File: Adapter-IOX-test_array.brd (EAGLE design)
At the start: 111.8 x 111.8 mm, 204 parts, among them Q0X11 P-FET, Q0X12 P-FET, Q0X13 P-FET, Q0X14 P-FET, Q10X11 P-FET, Q10X12 P-FET, Q10X13 P-FET, Q10X14 P-FET, Q11X11 P-FET, Q11X12 P-FET, Q11X13 P-FET, Q11X14 P-FET, Q12X11 P-FET, Q12X12 P-FET, Q12X13 P-FET, Q12X14 P-FET, Q13X11 P-FET, Q13X12 P-FET, Q13X13 P-FET, Q13X14 P-FET, Q14X11 P-FET, Q14X12 P-FET, Q14X13 P-FET, Q14X14 P-FET, Q15X11 P-FET, Q15X12 P-FET, Q15X13 P-FET, Q15X14 P-FET, Q1X11 P-FET, Q1X12 P-FET, Q1X13 P-FET, Q1X14 P-FET, Q2X11 P-FET, Q2X12 P-FET, Q2X13 P-FET, Q2X14 P-FET, Q3X11 P-FET, Q3X12 P-FET, Q3X13 P-FET, Q3X14 P-FET, Q4X11 P-FET, Q4X12 P-FET, Q4X13 P-FET, Q4X14 P-FET, Q5X11 P-FET, Q5X12 P-FET, Q5X13 P-FET, Q5X14 P-FET, Q6X11 P-FET, Q6X12 P-FET, Q6X13 P-FET, Q6X14 P-FET, Q7X11 P-FET, Q7X12 P-FET, Q7X13 P-FET, Q7X14 P-FET, Q8X11 P-FET, Q8X12 P-FET, Q8X13 P-FET, Q8X14 P-FET, Q9X11 P-FET, Q9X12 P-FET, Q9X13 P-FET, Q9X14 P-FET

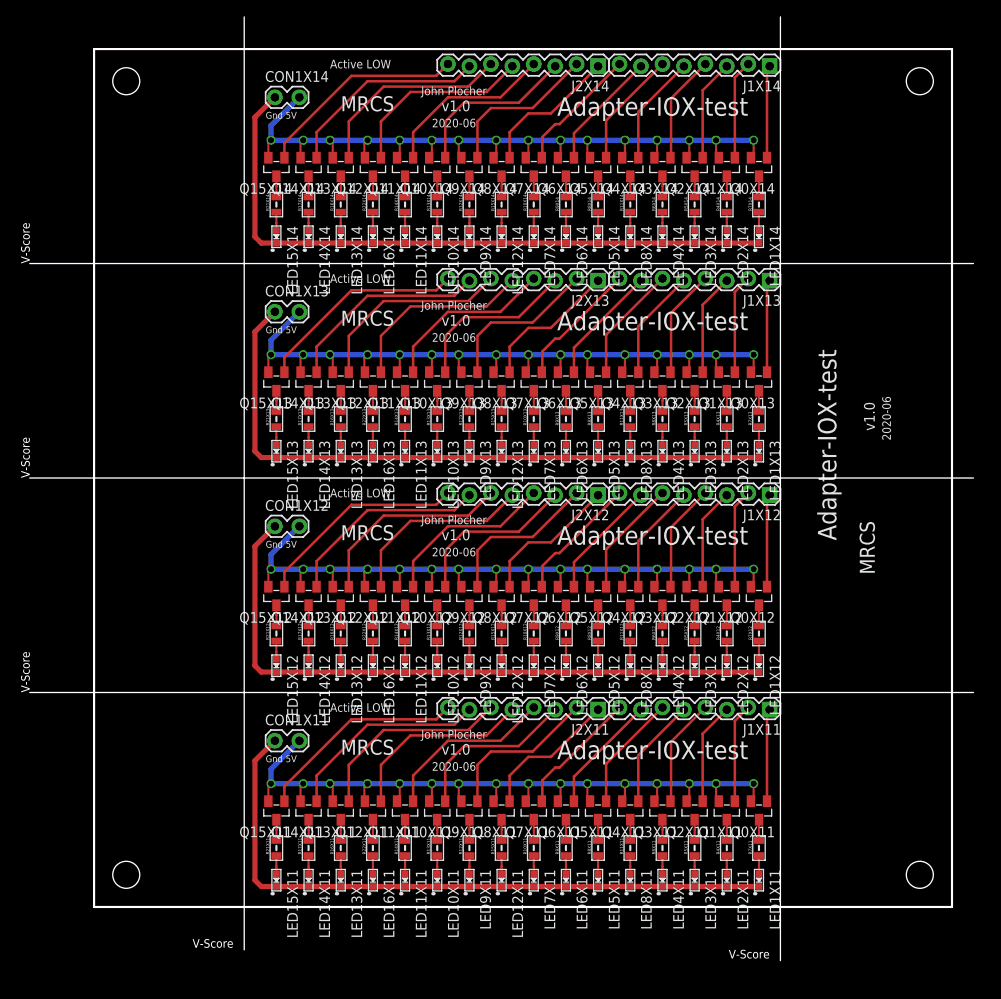
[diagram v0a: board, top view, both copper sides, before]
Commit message: higher density, narrow the board so 2x work with IOX-32
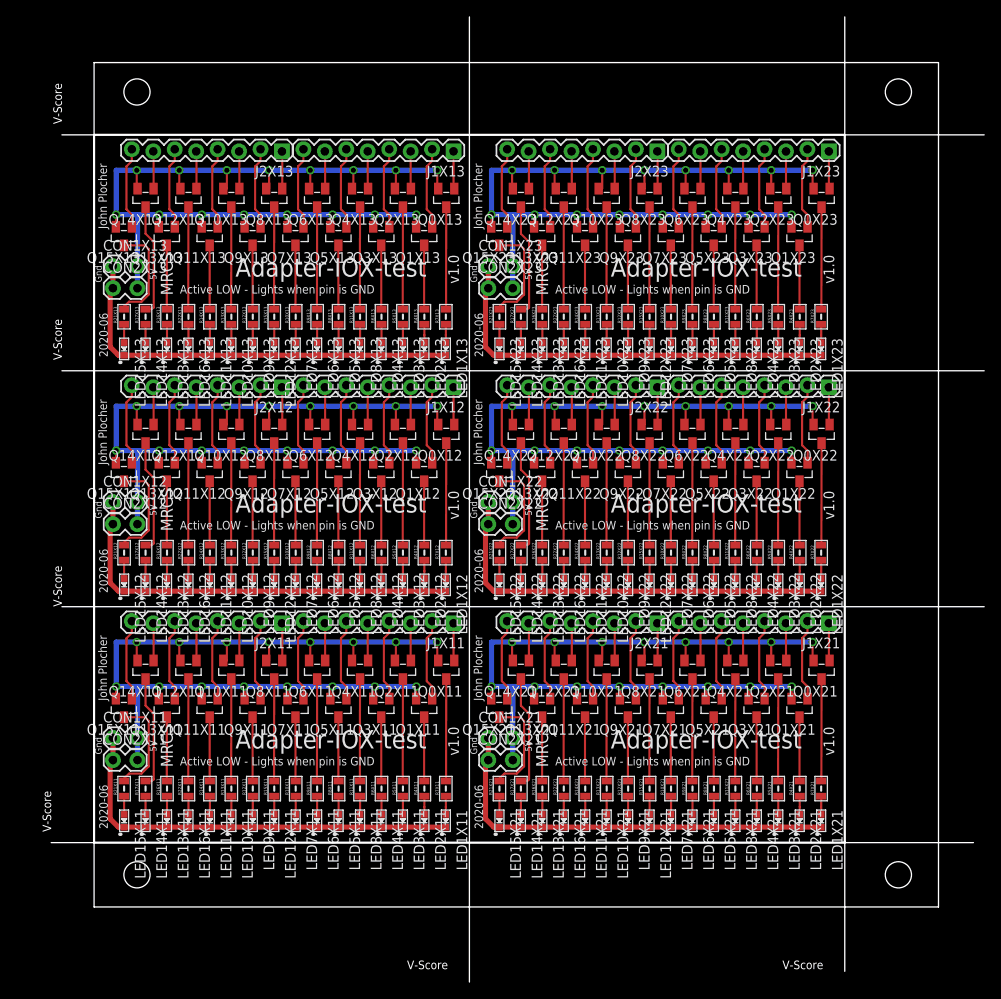
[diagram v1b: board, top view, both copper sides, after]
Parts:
- removed CON1X14: (no value), SPCoast:1X02_LOCK
- removed J1X14, J2X14: (no value), SPCoast:1X08_LOCK
- removed LED10X14, LED11X14, LED12X14, LED13X14, LED14X14, LED15X14, LED16X14, LED1X14, LED2X14, LED3X14, LED4X14, LED5X14, LED6X14, LED7X14, LED8X14, LED9X14: Y, SPCoast:0603-LED
- removed Q0X14, Q10X14, Q11X14, Q12X14, Q13X14, Q14X14, Q15X14, Q1X14, Q2X14, Q3X14, Q4X14, Q5X14, Q6X14, Q7X14, Q8X14, Q9X14: P-FET, SPCoast:SOT23
- removed R10X14, R11X14, R12X14, R13X14, R14X14, R15X14, R16X14, R17X14, R21X14, R22X14, R4X14, R5X14, R6X14, R7X14, R8X14, R9X14: 2K0, SPCoast:0805-RES
- added CON1X21, CON1X22, CON1X23, CON2X11, CON2X12, CON2X13, CON2X21, CON2X22, CON2X23: (no value), SPCoast:1X02_LOCK
- added J1X21, J1X22, J1X23, J2X21, J2X22, J2X23: (no value), SPCoast:1X08_LOCK
- added LED10X21, LED10X22, LED10X23, LED11X21, LED11X22, LED11X23, LED12X21, LED12X22, LED12X23, LED13X21, LED13X22, LED13X23, LED14X21, LED14X22, LED14X23, LED15X21, LED15X22, LED15X23, LED16X21, LED16X22, LED16X23, LED1X21, LED1X22, LED1X23, LED2X21, LED2X22, LED2X23, LED3X21, LED3X22, LED3X23, LED4X21, LED4X22, LED4X23, LED5X21, LED5X22, LED5X23, LED6X21, LED6X22, LED6X23, LED7X21, LED7X22, LED7X23, LED8X21, LED8X22, LED8X23, LED9X21, LED9X22, LED9X23: Y, SPCoast:0603-LED
- added Q0X21, Q0X22, Q0X23, Q10X21, Q10X22, Q10X23, Q11X21, Q11X22, Q11X23, Q12X21, Q12X22, Q12X23, Q13X21, Q13X22, Q13X23, Q14X21, Q14X22, Q14X23, Q15X21, Q15X22, Q15X23, Q1X21, Q1X22, Q1X23, Q2X21, Q2X22, Q2X23, Q3X21, Q3X22, Q3X23, Q4X21, Q4X22, Q4X23, Q5X21, Q5X22, Q5X23, Q6X21, Q6X22, Q6X23, Q7X21, Q7X22, Q7X23, Q8X21, Q8X22, Q8X23, Q9X21, Q9X22, Q9X23: P-FET, SPCoast:SOT23
- added R10X21, R10X22, R10X23, R11X21, R11X22, R11X23, R12X21, R12X22, R12X23, R13X21, R13X22, R13X23, R14X21, R14X22, R14X23, R15X21, R15X22, R15X23, R16X21, R16X22, R16X23, R17X21, R17X22, R17X23, R21X21, R21X22, R21X23, R22X21, R22X22, R22X23, R4X21, R4X22, R4X23, R5X21, R5X22, R5X23, R6X21, R6X22, R6X23, R7X21, R7X22, R7X23, R8X21, R8X22, R8X23, R9X21, R9X22, R9X23: 2K0, SPCoast:0805-RES
- added R22X1: (no value), SPCoast:BOARD-10X10-TEMPLATE
- moved Q0X13 42.9 mm to (41.7, 84.0)
- moved Q0X12 41.7 mm to (41.7, 56.0)
- moved Q2X13 40.8 mm to (36.6, 84.0)
- moved Q0X11 40.6 mm to (41.7, 28.1)
- moved J1X13 40.5 mm to (42.6, 89.6)
- moved J2X13 40.5 mm to (22.3, 89.6)
- moved Q1X13 39.8 mm to (39.1, 79.5)
- moved J1X12 39.6 mm to (42.6, 61.7)
- moved J2X12 39.6 mm to (22.3, 61.7)
- moved Q2X12 39.5 mm to (36.6, 56.0)
- moved LED1X13 39.0 mm to (41.7, 66.1)
- moved R7X13 39.0 mm to (41.7, 69.9)
- moved J1X11 38.8 mm to (42.6, 33.7)
- moved J2X11 38.8 mm to (22.3, 33.7)
- moved Q1X12 38.7 mm to (39.1, 51.5)
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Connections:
- removed net GNDX14: CON1X14.1, LED10X14.C, LED11X14.C, LED12X14.C, LED13X14.C, LED14X14.C, LED15X14.C, LED16X14.C, LED1X14.C, LED2X14.C, LED3X14.C, LED4X14.C, LED5X14.C, LED6X14.C, LED7X14.C, LED8X14.C, LED9X14.C
- removed net N$10X14: Q8X14.3, R15X14.2
- removed net N$11X14: Q9X14.3, R12X14.2
- removed net N$12X14: Q10X14.3, R13X14.2
- removed net N$13X14: Q11X14.3, R14X14.2
- removed net N$14X14: LED12X14.A, R15X14.1
- removed net N$15X14: LED9X14.A, R12X14.1
- removed net N$1X14: Q4X14.3, R11X14.2
- removed net N$23X14: LED10X14.A, R13X14.1
- removed net N$24X14: LED11X14.A, R14X14.1
- removed net N$28X14: Q12X14.3, R22X14.2
- removed net N$29X14: Q13X14.3, R16X14.2
- removed net N$30X14: Q14X14.3, R17X14.2
- removed net N$31X14: Q15X14.3, R21X14.2
- removed net N$32X14: LED16X14.A, R22X14.1
- removed net N$33X14: LED13X14.A, R16X14.1
- removed net N$34X14: LED14X14.A, R17X14.1
- removed net N$35X14: LED15X14.A, R21X14.1
- removed net N$3X14: Q5X14.3, R8X14.2
- removed net N$44X14: Q0X14.3, R7X14.2
- removed net N$45X14: Q1X14.3, R4X14.2
- removed net N$46X14: Q2X14.3, R5X14.2
- removed net N$47X14: Q3X14.3, R6X14.2
- removed net N$48X14: LED1X14.A, R7X14.1
- removed net N$49X14: LED2X14.A, R4X14.1
- removed net N$4X14: Q6X14.3, R9X14.2
- removed net N$50X14: LED3X14.A, R5X14.1
- removed net N$51X14: LED4X14.A, R6X14.1
- removed net N$5X14: Q7X14.3, R10X14.2
- removed net N$6X14: LED8X14.A, R11X14.1
- removed net N$7X14: LED5X14.A, R8X14.1
- removed net N$8X14: LED6X14.A, R9X14.1
- removed net N$9X14: LED7X14.A, R10X14.1
- removed net P10X14: J2X14.2, Q9X14.1
- removed net P11X14: J2X14.3, Q10X14.1
- removed net P12X14: J2X14.4, Q11X14.1
- removed net P13X14: J2X14.5, Q12X14.1
- removed net P14X14: J2X14.6, Q13X14.1
- removed net P15X14: J2X14.7, Q14X14.1
- removed net P16X14: J2X14.8, Q15X14.1
- removed net P1X14: J1X14.1, Q0X14.1
- removed net P2X14: J1X14.2, Q1X14.1
- removed net P3X14: J1X14.3, Q2X14.1
- removed net P4X14: J1X14.4, Q3X14.1
- removed net P5X14: J1X14.5, Q4X14.1
- removed net P6X14: J1X14.6, Q5X14.1
- removed net P7X14: J1X14.7, Q6X14.1
- removed net P8X14: J1X14.8, Q7X14.1
- removed net P9X14: J2X14.1, Q8X14.1
- removed net VCCX14: CON1X14.2, Q0X14.2, Q10X14.2, Q11X14.2, Q12X14.2, Q13X14.2, Q14X14.2, Q15X14.2, Q1X14.2, Q2X14.2, Q3X14.2, Q4X14.2, Q5X14.2, Q6X14.2, Q7X14.2, Q8X14.2, Q9X14.2
- new net GNDX21: CON1X21.1, CON2X21.1, LED10X21.C, LED11X21.C, LED12X21.C, LED13X21.C, LED14X21.C, LED15X21.C, LED16X21.C, LED1X21.C, LED2X21.C, LED3X21.C, LED4X21.C, LED5X21.C, LED6X21.C, LED7X21.C, LED8X21.C, LED9X21.C
- new net GNDX22: CON1X22.1, CON2X22.1, LED10X22.C, LED11X22.C, LED12X22.C, LED13X22.C, LED14X22.C, LED15X22.C, LED16X22.C, LED1X22.C, LED2X22.C, LED3X22.C, LED4X22.C, LED5X22.C, LED6X22.C, LED7X22.C, LED8X22.C, LED9X22.C
- new net GNDX23: CON1X23.1, CON2X23.1, LED10X23.C, LED11X23.C, LED12X23.C, LED13X23.C, LED14X23.C, LED15X23.C, LED16X23.C, LED1X23.C, LED2X23.C, LED3X23.C, LED4X23.C, LED5X23.C, LED6X23.C, LED7X23.C, LED8X23.C, LED9X23.C
- new net N$10X21: Q8X21.3, R15X21.2
- new net N$10X22: Q8X22.3, R15X22.2
- new net N$10X23: Q8X23.3, R15X23.2
- new net N$11X21: Q9X21.3, R12X21.2
- new net N$11X22: Q9X22.3, R12X22.2
- new net N$11X23: Q9X23.3, R12X23.2
- new net N$12X21: Q10X21.3, R13X21.2
- new net N$12X22: Q10X22.3, R13X22.2
- new net N$12X23: Q10X23.3, R13X23.2
- new net N$13X21: Q11X21.3, R14X21.2
- new net N$13X22: Q11X22.3, R14X22.2
- new net N$13X23: Q11X23.3, R14X23.2
- new net N$14X21: LED12X21.A, R15X21.1
- new net N$14X22: LED12X22.A, R15X22.1
- new net N$14X23: LED12X23.A, R15X23.1
- new net N$15X21: LED9X21.A, R12X21.1
- new net N$15X22: LED9X22.A, R12X22.1
- new net N$15X23: LED9X23.A, R12X23.1
- new net N$1X21: Q4X21.3, R11X21.2
- new net N$1X22: Q4X22.3, R11X22.2
- new net N$1X23: Q4X23.3, R11X23.2
- new net N$23X21: LED10X21.A, R13X21.1
- new net N$23X22: LED10X22.A, R13X22.1
- new net N$23X23: LED10X23.A, R13X23.1
- new net N$24X21: LED11X21.A, R14X21.1
- new net N$24X22: LED11X22.A, R14X22.1
- new net N$24X23: LED11X23.A, R14X23.1
- new net N$28X21: Q12X21.3, R22X21.2
- new net N$28X22: Q12X22.3, R22X22.2
- new net N$28X23: Q12X23.3, R22X23.2
- new net N$29X21: Q13X21.3, R16X21.2
- new net N$29X22: Q13X22.3, R16X22.2
- new net N$29X23: Q13X23.3, R16X23.2
- new net N$30X21: Q14X21.3, R17X21.2
- new net N$30X22: Q14X22.3, R17X22.2
- new net N$30X23: Q14X23.3, R17X23.2
- new net N$31X21: Q15X21.3, R21X21.2
- new net N$31X22: Q15X22.3, R21X22.2
- new net N$31X23: Q15X23.3, R21X23.2
- new net N$32X21: LED16X21.A, R22X21.1
- new net N$32X22: LED16X22.A, R22X22.1
- new net N$32X23: LED16X23.A, R22X23.1
- new net N$33X21: LED13X21.A, R16X21.1
- new net N$33X22: LED13X22.A, R16X22.1
- new net N$33X23: LED13X23.A, R16X23.1
- new net N$34X21: LED14X21.A, R17X21.1
- new net N$34X22: LED14X22.A, R17X22.1
- new net N$34X23: LED14X23.A, R17X23.1
- new net N$35X21: LED15X21.A, R21X21.1
- new net N$35X22: LED15X22.A, R21X22.1
- new net N$35X23: LED15X23.A, R21X23.1
- new net N$3X21: Q5X21.3, R8X21.2
- new net N$3X22: Q5X22.3, R8X22.2
- new net N$3X23: Q5X23.3, R8X23.2
- new net N$44X21: Q0X21.3, R7X21.2
- new net N$44X22: Q0X22.3, R7X22.2
- new net N$44X23: Q0X23.3, R7X23.2
- new net N$45X21: Q1X21.3, R4X21.2
- new net N$45X22: Q1X22.3, R4X22.2
- new net N$45X23: Q1X23.3, R4X23.2
- new net N$46X21: Q2X21.3, R5X21.2
- new net N$46X22: Q2X22.3, R5X22.2
- new net N$46X23: Q2X23.3, R5X23.2
- new net N$47X21: Q3X21.3, R6X21.2
- new net N$47X22: Q3X22.3, R6X22.2
- new net N$47X23: Q3X23.3, R6X23.2
- new net N$48X21: LED1X21.A, R7X21.1
- new net N$48X22: LED1X22.A, R7X22.1
- new net N$48X23: LED1X23.A, R7X23.1
- new net N$49X21: LED2X21.A, R4X21.1
- new net N$49X22: LED2X22.A, R4X22.1
- new net N$49X23: LED2X23.A, R4X23.1
- new net N$4X21: Q6X21.3, R9X21.2
- new net N$4X22: Q6X22.3, R9X22.2
- new net N$4X23: Q6X23.3, R9X23.2
- new net N$50X21: LED3X21.A, R5X21.1
- new net N$50X22: LED3X22.A, R5X22.1
- new net N$50X23: LED3X23.A, R5X23.1
- new net N$51X21: LED4X21.A, R6X21.1
- new net N$51X22: LED4X22.A, R6X22.1
- new net N$51X23: LED4X23.A, R6X23.1
- new net N$5X21: Q7X21.3, R10X21.2
- new net N$5X22: Q7X22.3, R10X22.2
- new net N$5X23: Q7X23.3, R10X23.2
- new net N$6X21: LED8X21.A, R11X21.1
- new net N$6X22: LED8X22.A, R11X22.1
- new net N$6X23: LED8X23.A, R11X23.1
- new net N$7X21: LED5X21.A, R8X21.1
- new net N$7X22: LED5X22.A, R8X22.1
- new net N$7X23: LED5X23.A, R8X23.1
- new net N$8X21: LED6X21.A, R9X21.1
- new net N$8X22: LED6X22.A, R9X22.1
- new net N$8X23: LED6X23.A, R9X23.1
- new net N$9X21: LED7X21.A, R10X21.1
- new net N$9X22: LED7X22.A, R10X22.1
- new net N$9X23: LED7X23.A, R10X23.1
- new net P10X21: J2X21.2, Q9X21.1
- new net P10X22: J2X22.2, Q9X22.1
- new net P10X23: J2X23.2, Q9X23.1
- new net P11X21: J2X21.3, Q10X21.1
- new net P11X22: J2X22.3, Q10X22.1
- new net P11X23: J2X23.3, Q10X23.1
- new net P12X21: J2X21.4, Q11X21.1
- new net P12X22: J2X22.4, Q11X22.1
- new net P12X23: J2X23.4, Q11X23.1
- new net P13X21: J2X21.5, Q12X21.1
- new net P13X22: J2X22.5, Q12X22.1
- new net P13X23: J2X23.5, Q12X23.1
- new net P14X21: J2X21.6, Q13X21.1
- new net P14X22: J2X22.6, Q13X22.1
- new net P14X23: J2X23.6, Q13X23.1
- new net P15X21: J2X21.7, Q14X21.1
- new net P15X22: J2X22.7, Q14X22.1
- new net P15X23: J2X23.7, Q14X23.1
- new net P16X21: J2X21.8, Q15X21.1
- new net P16X22: J2X22.8, Q15X22.1
- new net P16X23: J2X23.8, Q15X23.1
- new net P1X21: J1X21.1, Q0X21.1
- new net P1X22: J1X22.1, Q0X22.1
- new net P1X23: J1X23.1, Q0X23.1
- new net P2X21: J1X21.2, Q1X21.1
- new net P2X22: J1X22.2, Q1X22.1
- new net P2X23: J1X23.2, Q1X23.1
- new net P3X21: J1X21.3, Q2X21.1
- new net P3X22: J1X22.3, Q2X22.1
- new net P3X23: J1X23.3, Q2X23.1
- new net P4X21: J1X21.4, Q3X21.1
- new net P4X22: J1X22.4, Q3X22.1
- new net P4X23: J1X23.4, Q3X23.1
- new net P5X21: J1X21.5, Q4X21.1
- new net P5X22: J1X22.5, Q4X22.1
- new net P5X23: J1X23.5, Q4X23.1
- new net P6X21: J1X21.6, Q5X21.1
- new net P6X22: J1X22.6, Q5X22.1
- new net P6X23: J1X23.6, Q5X23.1
- new net P7X21: J1X21.7, Q6X21.1
- new net P7X22: J1X22.7, Q6X22.1
- new net P7X23: J1X23.7, Q6X23.1
- new net P8X21: J1X21.8, Q7X21.1
- new net P8X22: J1X22.8, Q7X22.1
- new net P8X23: J1X23.8, Q7X23.1
- new net P9X21: J2X21.1, Q8X21.1
- new net P9X22: J2X22.1, Q8X22.1
- new net P9X23: J2X23.1, Q8X23.1
- new net VCCX21: CON1X21.2, CON2X21.2, Q0X21.2, Q10X21.2, Q11X21.2, Q12X21.2, Q13X21.2, Q14X21.2, Q15X21.2, Q1X21.2, Q2X21.2, Q3X21.2, Q4X21.2, Q5X21.2, Q6X21.2, Q7X21.2, Q8X21.2, Q9X21.2
- new net VCCX22: CON1X22.2, CON2X22.2, Q0X22.2, Q10X22.2, Q11X22.2, Q12X22.2, Q13X22.2, Q14X22.2, Q15X22.2, Q1X22.2, Q2X22.2, Q3X22.2, Q4X22.2, Q5X22.2, Q6X22.2, Q7X22.2, Q8X22.2, Q9X22.2
- new net VCCX23: CON1X23.2, CON2X23.2, Q0X23.2, Q10X23.2, Q11X23.2, Q12X23.2, Q13X23.2, Q14X23.2, Q15X23.2, Q1X23.2, Q2X23.2, Q3X23.2, Q4X23.2, Q5X23.2, Q6X23.2, Q7X23.2, Q8X23.2, Q9X23.2
- net GNDX11: now also CON2X11.1
- net GNDX12: now also CON2X12.1
- net GNDX13: now also CON2X13.1
- net VCCX11: now also CON2X11.2
- net VCCX12: now also CON2X12.2
- net VCCX13: now also CON2X13.2
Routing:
- net VCCX22: track 0.00 -> 118.6 mm, vias 0 -> 16
- net VCCX23: track 0.00 -> 118.6 mm, vias 0 -> 16
- net VCCX21: track 0.00 -> 118.6 mm, vias 0 -> 16
- net VCCX14: track 112.6 -> 0.00 mm, vias 16 -> 0
- net GNDX14: track 77.5 -> 0.00 mm
- net GNDX23: track 0.00 -> 50.0 mm
- net GNDX22: track 0.00 -> 50.0 mm
- net GNDX21: track 0.00 -> 50.0 mm
- net GNDX11: track 77.5 -> 50.0 mm
- net GNDX13: track 77.5 -> 50.0 mm
- net GNDX12: track 77.5 -> 50.0 mm
- net P16X14: track 25.1 -> 0.00 mm
- net P15X14: track 24.4 -> 0.00 mm
- net P14X14: track 23.9 -> 0.00 mm
- net P13X14: track 22.6 -> 0.00 mm
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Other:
- board size 111.8 x 111.8 mm -> 110.5 x 114.3 mm
- board text added: "5V"
- board text added: "5V GND"
- board text added: "Active LOW - Lights when pin is GND"
- board text added: "Gnd"
- board text removed: "Active LOW"
- board text removed: "Gnd 5V"

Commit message: updated docs
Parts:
- added FID1, FID2, FID3, FID4: (no value), SPCoast:FIDUCIAL_1MM
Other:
- outline, holes or cut-outs redrawn
- board text added: "(0,0)"
- board text added: "Feed"

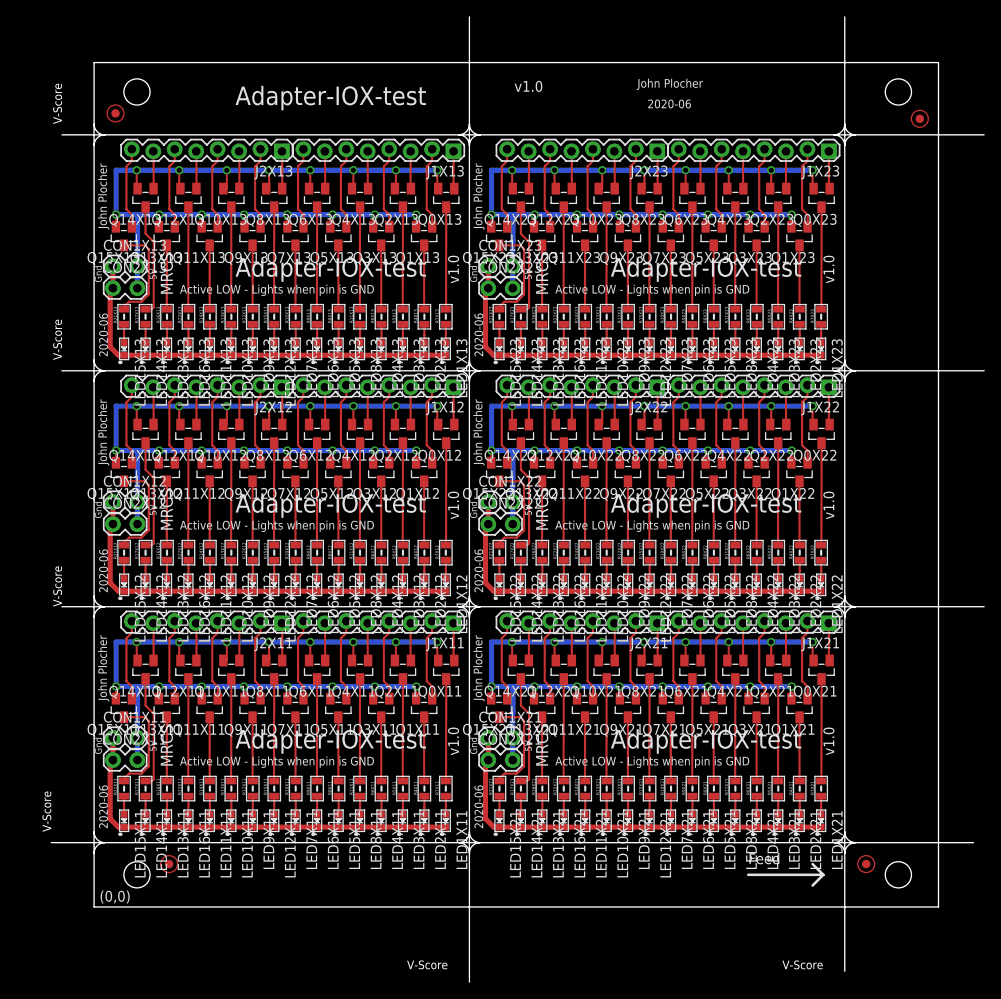
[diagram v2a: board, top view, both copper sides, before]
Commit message: fixed SPCoast lbr part orientation
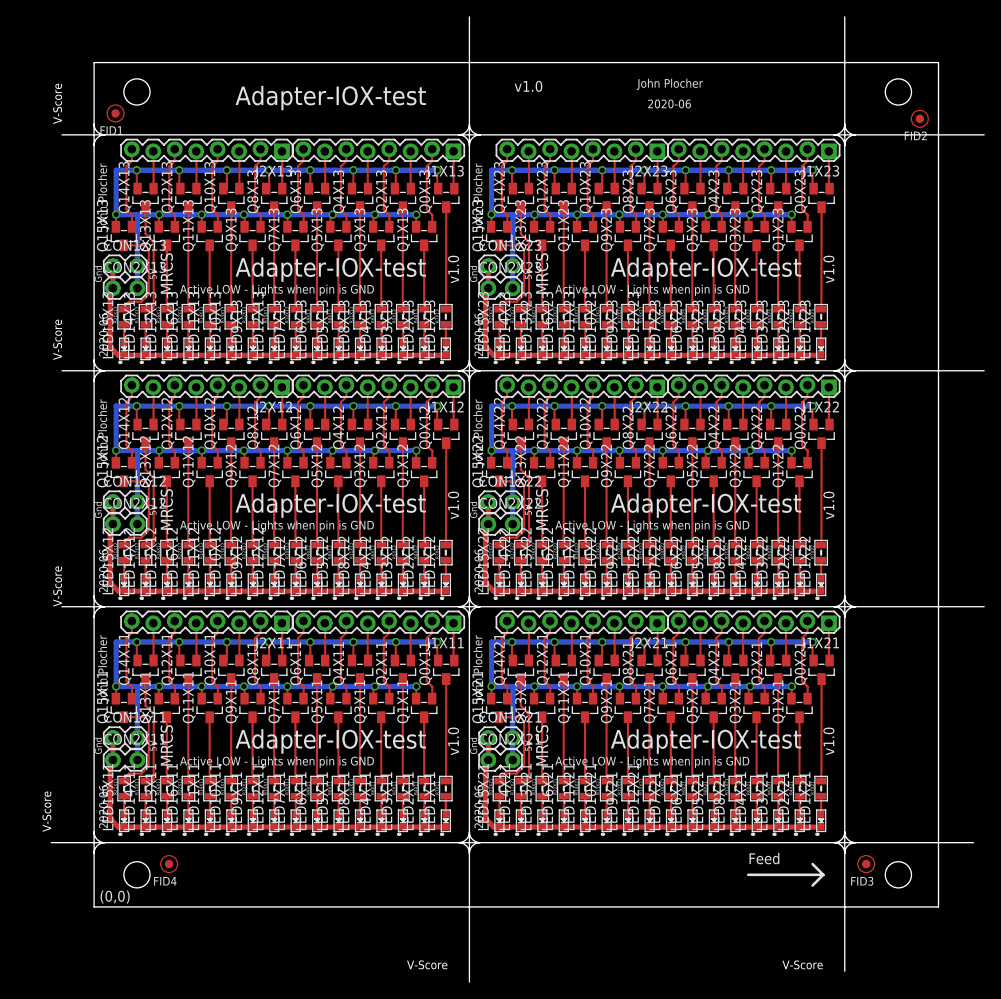
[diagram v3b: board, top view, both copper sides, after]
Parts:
- turned LED10X11 to 90 degrees
- turned LED10X12 to 90 degrees
- turned LED10X13 to 90 degrees
- turned LED10X21 to 90 degrees
- turned LED10X22 to 90 degrees
- turned LED10X23 to 90 degrees
- turned LED11X11 to 90 degrees
- turned LED11X12 to 90 degrees
- turned LED11X13 to 90 degrees
- turned LED11X21 to 90 degrees
- turned LED11X22 to 90 degrees
- turned LED11X23 to 90 degrees
- turned LED12X11 to 90 degrees
- turned LED12X12 to 90 degrees
- turned LED12X13 to 90 degrees
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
